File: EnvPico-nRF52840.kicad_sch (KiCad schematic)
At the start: 48 parts, among them J3 2.54mm header 01x20, J4 2.54mm header 01x20, J5 Conn_01x03_Male, U1 LM3671MF 3.3, U2 BQ24072RGT, U3 nRF52840, Y1 32MHz 12pF

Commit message: changed 2012 crystal for a 3225 size due to part availability. + went through and did a general clean up and correction per DRC.
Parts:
- Y1: footprint Crystal:Crystal_SMD_2016-4Pin_2.0x1.6mm -> Crystal:Crystal_SMD_3225-4Pin_3.2x2.5mm
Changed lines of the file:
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@@
       (effects (font (size 1.27 1.27)) (justify right))
     )
-    (property "Footprint" "Crystal:Crystal_SMD_2016-4Pin_2.0x1.6mm" (id 2) (at 160.02 200.66 0)
+    (property "Footprint" "Crystal:Crystal_SMD_3225-4Pin_3.2x2.5mm" (id 2) (at 160.02 200.66 0)
       (effects (font (size 1.27 1.27)) hide)
     )
@@
     )
     (path "/00000000-0000-0000-0000-00006116f722"
-      (reference "Y1") (unit 1) (value "32MHz 12pF") (footprint "Crystal:Crystal_SMD_2016-4Pin_2.0x1.6mm")
+      (reference "Y1") (unit 1) (value "32MHz 12pF") (footprint "Crystal:Crystal_SMD_3225-4Pin_3.2x2.5mm")
     )
     (path "/00000000-0000-0000-0000-00005edb7d8d"

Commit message: fixed a kicad derp
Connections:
- no-connect marks 4 -> 6
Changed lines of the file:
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@@
   (junction (at 227.33 46.99) (diameter 1.016) (color 0 0 0 0))
   (junction (at 234.95 96.52) (diameter 1.016) (color 0 0 0 0))
+  (no_connect (at 27.94 35.56))
+  (no_connect (at 27.94 50.8))
   (no_connect (at 90.17 46.99))
   (no_connect (at 90.17 57.15))
@@
       (effects (font (size 1.27 1.27)) hide)
     )
-    (property "Value" "GND" (id 1) (at 323.2658 163.703 0))
+    (property "Value" "GND" (id 1) (at 323.2658 163.703 90))
     (property "Footprint" "" (id 2) (at 327.66 163.83 0)
       (effects (font (size 1.27 1.27)) hide)

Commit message: moved some traces about to make sure there is good ground coverage
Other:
- moved on the sheet: J3

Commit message: fixed leftover silkscreen C12, couple of plane tweaks and added center marker / board dimensions on back of PCB, fixed incorrect diode footprint and in schematic
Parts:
- D4: value Schottky 0603 -> 1N4002W; footprint Diode_SMD:D_0603_1608Metric -> Diode_SMD:D_SOD-123
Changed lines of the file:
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@@
     (in_bom yes) (on_board yes)
     (property "Reference" "D4" (id 0) (at 62.23 38.9382 0))
-    (property "Value" "Schottky 0603" (id 1) (at 62.23 41.2496 0))
-    (property "Footprint" "Diode_SMD:D_0603_1608Metric" (id 2) (at 62.23 44.45 0)
+    (property "Value" "1N4002W" (id 1) (at 62.23 41.2496 0))
+    (property "Footprint" "Diode_SMD:D_SOD-123" (id 2) (at 62.23 44.45 0)
       (effects (font (size 1.27 1.27)) hide)
     )
@@
     )
     (path "/00000000-0000-0000-0000-000061233dc7"
-      (reference "D4") (unit 1) (value "Schottky 0603") (footprint "Diode_SMD:D_0603_1608Metric")
+      (reference "D4") (unit 1) (value "1N4002W") (footprint "Diode_SMD:D_SOD-123")
     )
     (path "/00000000-0000-0000-0000-0000611692b8"

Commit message: added silkscreen pin labels to the bottom of the PCB
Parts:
- renumbered e1 to USB1
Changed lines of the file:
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@@
   (symbol (lib_id "Type-C:HRO-TYPE-C-31-M-12") (at 25.4 44.45 0) (unit 1)
     (in_bom yes) (on_board yes)
-    (property "Reference" "e1" (id 0) (at 19.05 34.29 0)
+    (property "Reference" "USB1" (id 0) (at 19.05 34.29 0)
       (effects (font (size 1.27 1.27)) (justify right))
     )
@@
       (reference "U3") (unit 1) (value "nRF52840") (footprint "Package_DFN_QFN:Nordic_AQFN-73-1EP_7x7mm_P0.5mm")
     )
+    (path "/00000000-0000-0000-0000-00005edb7d8d"
+      (reference "USB1") (unit 1) (value "TYPE-C-31-M-12") (footprint "HRO-TYPE-C31-M-12:HRO-TYPE-C-31-M-12")
+    )
     (path "/00000000-0000-0000-0000-00006116f722"
       (reference "Y1") (unit 1) (value "32MHz 12pF") (footprint "Crystal:Crystal_SMD_3225-4Pin_3.2x2.5mm")
     )
-    (path "/00000000-0000-0000-0000-00005edb7d8d"
-      (reference "e1") (unit 1) (value "TYPE-C-31-M-12") (footprint "HRO-TYPE-C31-M-12:HRO-TYPE-C-31-M-12")
-    )
   )

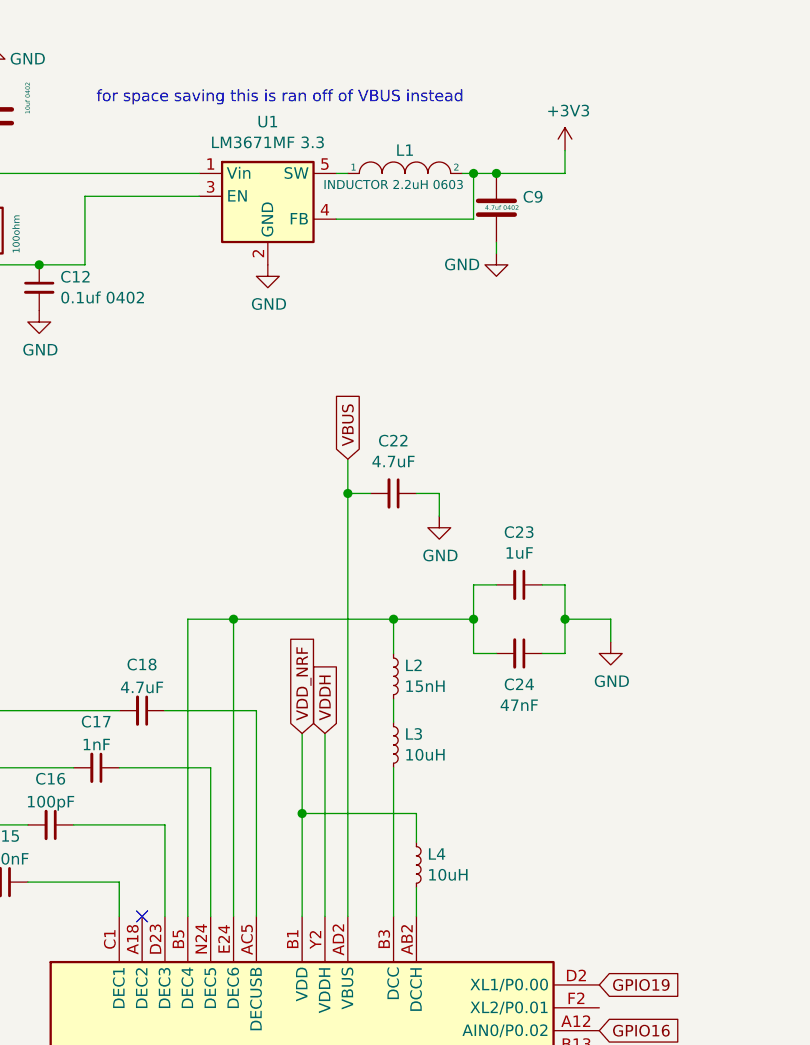
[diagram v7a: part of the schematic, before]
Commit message: I think this is correct trace thickness for 50ohm impedance
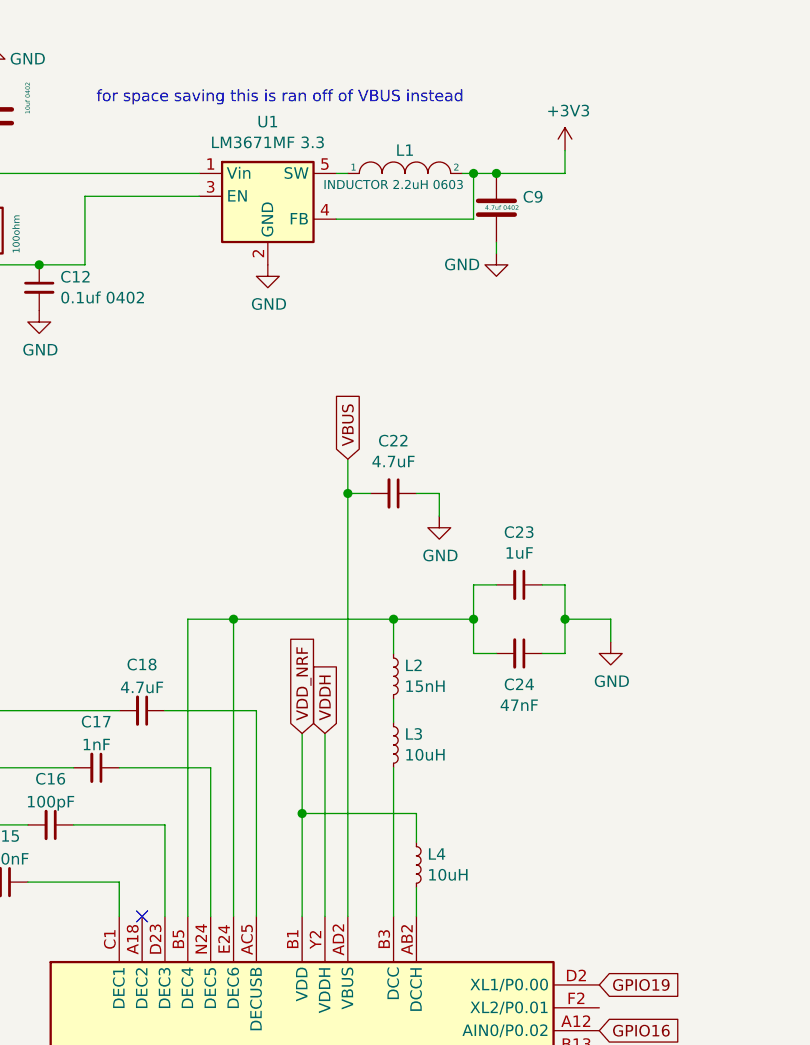
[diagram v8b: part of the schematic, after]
